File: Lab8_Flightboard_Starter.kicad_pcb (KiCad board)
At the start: 2 copper layers, 80 x 80 mm, 64 parts, among them J10 ESC3_GND, J11 ESC4_VBAT, J12 ESC4_GND, J5 ESC1_VBAT, J6 ESC1_GND, J7 ESC2_VBAT, J8 ESC2_GND, J9 ESC3_VBAT, M1 Motor1, M2 Motor2, M3 Motor3, M4 Motor4, Q1 DMP6023LE-13, U2 TPS62933, U4 LP5912-3.3DRV, U5 LP5912-3.3DRV, U6 NRF24L01_Breakout

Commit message: More traces
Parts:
- moved D6 38.2 mm to (130.0, 93.5), turned to 0 degrees
- moved D3 33.7 mm to (162.5, 103.5)
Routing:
- net /SCK: track 0.00 -> 55.8 mm, vias 0 -> 8
- net /CS: track 0.00 -> 52.0 mm, vias 0 -> 6
- net /3.3V_IMU: track 0.00 -> 47.1 mm
- net /M2_CMD: track 0.00 -> 37.2 mm, vias 0 -> 3
- net /M1_CMD: track 0.00 -> 36.7 mm, vias 0 -> 2
- net /MOSI: track 0.00 -> 22.5 mm, vias 0 -> 2
- net /5V_OUT: track 83.5 -> 106.0 mm
- net /3.3V_GP: track 0.00 -> 17.7 mm
- net /MISO: track 0.00 -> 14.1 mm, vias 0 -> 3
- net /MOTOR2: track 0.00 -> 9.83 mm
- net /ADC3: track 0.00 -> 9.70 mm
- net /MOTOR1: track 0.00 -> 8.21 mm
- net Net-(D3-A): track 0.00 -> 2.97 mm
- net Net-(D6-A): track 0.00 -> 2.64 mm

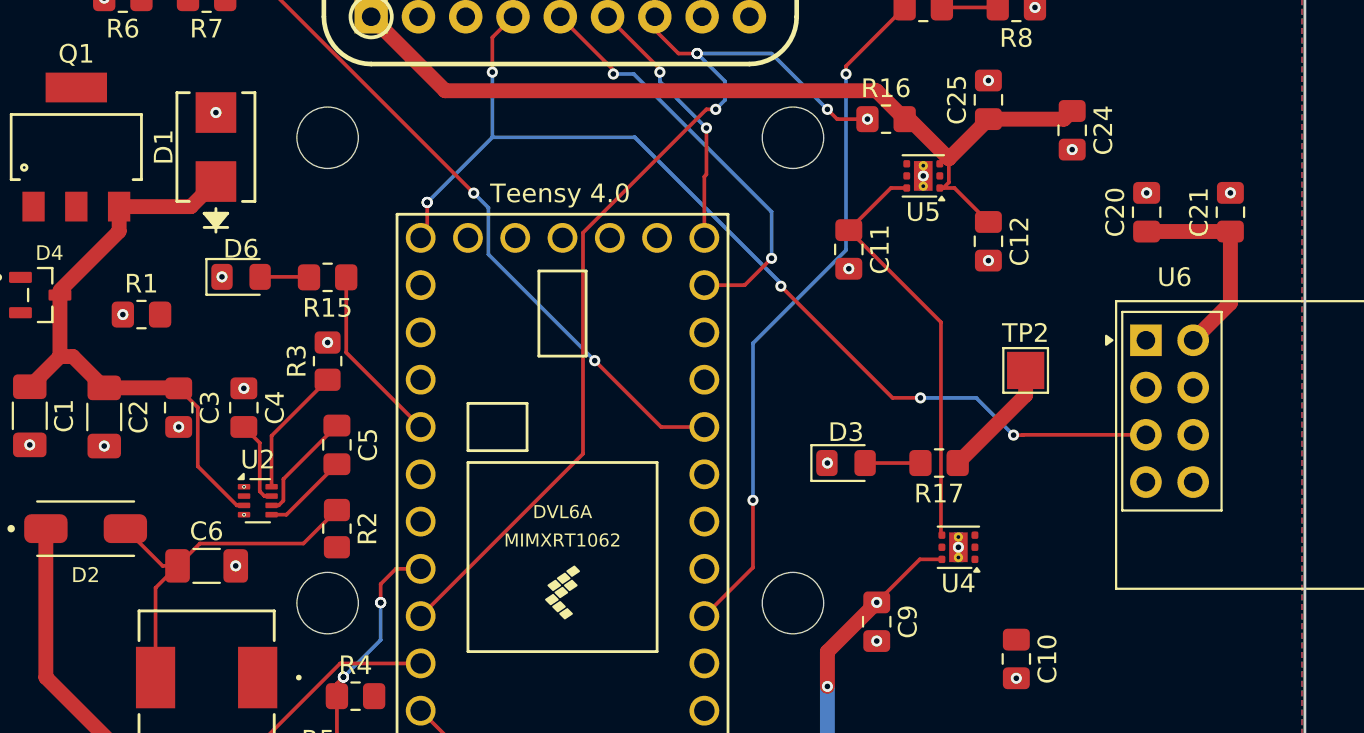
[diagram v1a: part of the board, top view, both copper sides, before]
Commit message: Added all traces (errors still)
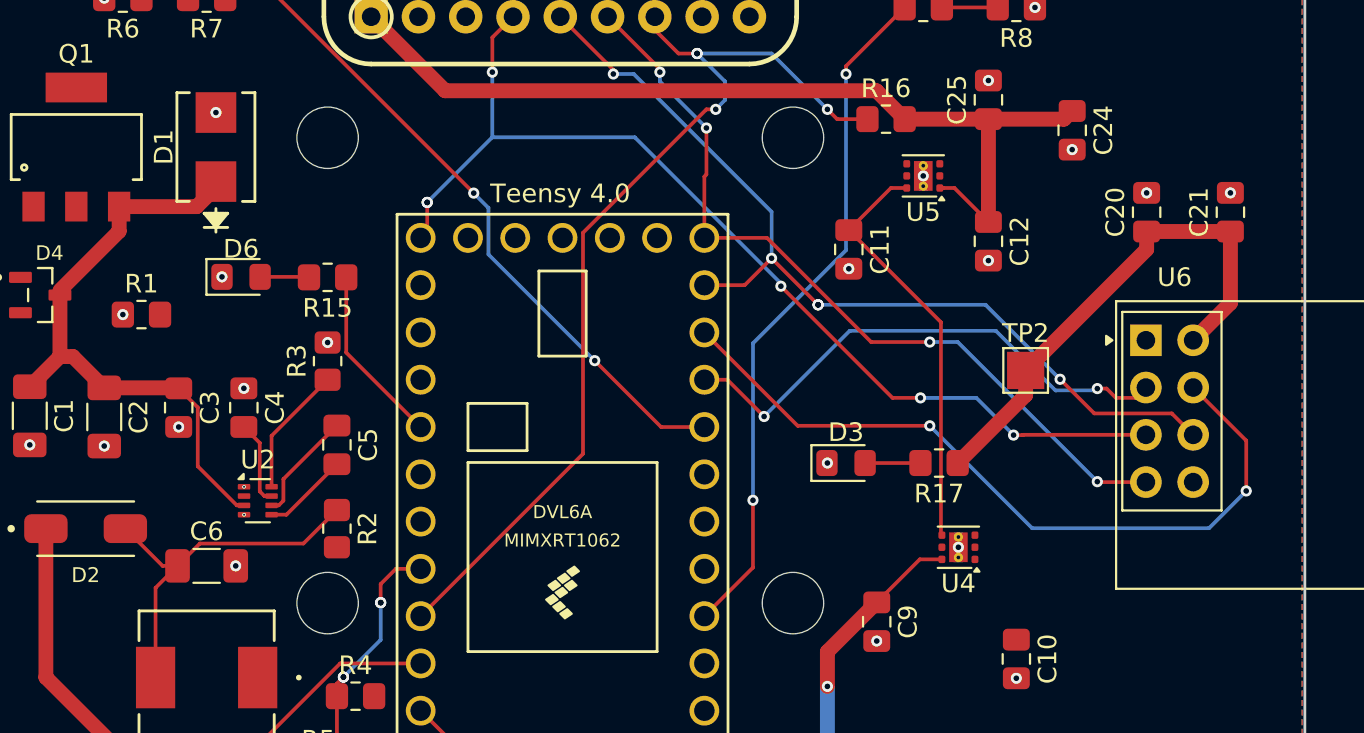
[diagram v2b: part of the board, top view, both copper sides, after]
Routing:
- net /CSN: track 0.00 -> 41.0 mm, vias 0 -> 2
- net /MISO: track 14.1 -> 43.3 mm, vias 3 -> 4
- net /CE: track 0.00 -> 28.2 mm, vias 0 -> 2
- net /MOSI: track 22.5 -> 49.1 mm, vias 2 -> 5
- net /3.3V_GP: track 17.7 -> 27.8 mm
- net /3.3V_IMU: track 47.1 -> 49.2 mm
- net /SCK: vias 8 -> 6
- net /M2_CMD: vias 3 -> 2
- net /CS: vias 6 -> 5
- net /5V_OUT: vias 5 -> 4

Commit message: Fixed most errors
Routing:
- net /VBAT: track 0.00 -> 16.5 mm
- net /3.3V_GP: track 27.8 -> 41.3 mm
- net Net-(D4-~-Pad1): track 0.00 -> 13.3 mm, vias 0 -> 2
- net Net-(U2-SW): track 4.63 -> 13.5 mm, vias 0 -> 2
- net /MOTOR3: track 2.00 -> 7.68 mm
- net Net-(U2-BST): track 5.96 -> 11.6 mm
- net Net-(U2-FB): track 7.00 -> 12.4 mm, vias 0 -> 2
- net GND: track 0.00 -> 4.53 mm
- net /CE: track 28.2 -> 32.5 mm
- net /5V_OUT: track 106.0 -> 109.4 mm
- net /VBAT_SENSE: vias 4 -> 2
- net /SCK: vias 6 -> 5
- net /MOSI: vias 5 -> 4
- net /CS: vias 5 -> 3

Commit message: Fixed all errors
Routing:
- net /VBAT: track 16.5 -> 33.3 mm, vias 0 -> 2
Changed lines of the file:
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@@
 	)
 	(segment
-		(start 121.15 83.325)
-		(end 112.3 92.175)
+		(start 118.65 134.025)
+		(end 125.475 134.025)
 		(width 0.8)
 		(layer "F.Cu")
@@
 	)
 	(segment
-		(start 112.3 92.175)
-		(end 112.3 96.125)
-		(width 0.8)
-		(layer "F.Cu")
+		(start 116.5 131.875)
+		(end 118.65 134.025)
+		(width 0.8)
+		(layer "F.Cu")
+		(net "/VBAT")
+	)
+	(segment
+		(start 125.475 134.025)
+		(end 134 125.5)
+		(width 0.8)
+		(layer "F.Cu")
+		(net "/VBAT")
+	)
+	(segment
+		(start 134 125.5)
+		(end 135 125.5)
+		(width 0.8)
+		(layer "F.Cu")
+		(net "/VBAT")
+	)
+	(segment
+		(start 137.15 116.025)
+		(end 137.15 120.35)
+		(width 0.8)
+		(layer "F.Cu")
+		(net "/VBAT")
+	)
+	(segment
+		(start 137.15 120.35)
+		(end 137 120.5)
+		(width 0.2)
+		(layer "F.Cu")
+		(net "/VBAT")
+	)
+	(via
+		(at 137 120.5)
+		(size 0.6)
+		(drill 0.3)
+		(layers "F.Cu" "B.Cu")
+		(net "/VBAT")
+	)
+	(via
+		(at 135 125.5)
+		(size 0.6)
+		(drill 0.3)
+		(layers "F.Cu" "B.Cu")
+		(net "/VBAT")
+	)
+	(segment
+		(start 135.5 125)
+		(end 135 125.5)
+		(width 0.8)
+		(layer "B.Cu")
+		(net "/VBAT")
+	)
+	(segment
+		(start 137 120.5)
+		(end 135.5 122)
+		(width 0.8)
+		(layer "B.Cu")
+		(net "/VBAT")
+	)
+	(segment
+		(start 135.5 122)
+		(end 135.5 125)
+		(width 0.8)
+		(layer "B.Cu")
 		(net "/VBAT")
 	)
@@
 		(polygon
 			(pts
-				(xy 107 59.5) (xy 108 58.5) (xy 186.5 58.5) (xy 187 59.5) (xy 187 138) (xy 186 138.5) (xy 108 138.5)
+				(xy 107 59.5) (xy 108 58.5) (xy 186.5 58.5) (xy 187 59.5) (xy 187 137.5) (xy 186 138.5) (xy 108 138.5)
 				(xy 107 137.5)
 			)

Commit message: Added BOM and gerber
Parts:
- renumbered LSM to U9
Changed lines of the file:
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@@
 		(descr "Adafruit LSM6DSO32 6-DoF IMU breakout, product 4692; 25.4 x 17.78 mm; 1x9 primary and 1x5 auxiliary 2.54 mm headers.")
 		(tags "Adafruit LSM6DSO32 breakout IMU I2C SPI STEMMA QT")
-		(property "Reference" "LSM"
+		(property "Reference" "U9"
 			(at 0 -10.4 0)
 			(layer "F.SilkS")

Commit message: Fixed values
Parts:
- L1: value 3.3u -> 4.7u
- U1: renamed from Teensy 4.0
- renumbered M1 to J1, M2 to J2, M3 to J3, M4 to J4

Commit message: Edited formatting and remade BOM
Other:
- board text added: "LP"
- board text added: "LSM"
- board text added: "Motor1"
- board text added: "Motor2"
- board text added: "Motor3"
- board text added: "Motor4"
- board text added: "NRF"
- board text added: "TPS"
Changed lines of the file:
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@@
 		(tags "nRF24L01 adapter breakout")
 		(property "Reference" "U6"
-			(at 1.54 -3.38 0)
+			(at 1.54 -2.905 0)
 			(layer "F.SilkS")
+			(hide yes)
 			(effects
 				(font
@@
 			(at 2.475 2.5 0)
 			(layer "F.SilkS")
+			(hide yes)
 			(effects
 				(font
@@
 		(tags "resistor handsolder")
 		(property "Reference" "R17"
-			(at 0 -1.65 0)
+			(at 0 1.5 0)
 			(layer "F.SilkS")
 			(effects
@@
 		(tags "capacitor handsolder")
 		(property "Reference" "C15"
-			(at 0 -1.68 90)
+			(at 0 1.65 90)
 			(layer "F.SilkS")
 			(effects
@@
 		(tags "capacitor handsolder")
 		(property "Reference" "C1"
-			(at 0 -1.85 90)
+			(at -2.9625 0.05 180)
 			(layer "F.SilkS")
 			(effects
@@
 		(tags "capacitor handsolder")
 		(property "Reference" "C10"
-			(at 0 -1.68 90)
+			(at 0 1.65 90)
 			(layer "F.SilkS")
 			(effects
@@
 			(at 0 -2.225 0)
 			(layer "F.SilkS")
+			(hide yes)
 			(effects
 				(font
@@
 			(layer "F.Fab")
 		)
-		(fp_text user "${REFERENCE}"
-			(at 0 0 0)
-			(layer "F.Fab")
-			(effects
-				(font
-					(size 0.5 0.5)
-					(thickness 0.08)
-				)
-			)
-		)
 		(pad "" smd roundrect
 			(at 0 -0.4 180)
@@
 		(tags "resistor handsolder")
 		(property "Reference" "R8"
-			(at 0 -1.65 0)
+			(at 0.15 1.525 0)
 			(layer "F.SilkS")
 			(effects
@@
 		(tags "capacitor handsolder")
 		(property "Reference" "C3"
-			(at 0 -1.68 90)
+			(at -2.525 0.05 180)
 			(layer "F.SilkS")
 			(effects
@@
 			(at 0 -10.4 0)
 			(layer "F.SilkS")
+			(hide yes)
 			(effects
 				(font
@@
 			)
 		)
-		(property "Datasheet" "https://www.adafruit.com/product/4692"
+		(property "Datasheet" ""
 			(at 0 0 0)
 			(layer "F.Fab")
@@
 			)
 		)
-		(property "Description" "Adafruit LSM6DSO32 6-DoF accelerometer/gyroscope breakout; I2C/SPI, STEMMA QT, primary and auxiliary headers."
+		(property "Description" ""
 			(at 0 0 0)
 			(layer "F.Fab")
@@
 		(tags "capacitor handsolder")
 		(property "Reference" "C2"
-			(at 0 -1.85 90)
+			(at -3.025 0.05 180)
 			(layer "F.SilkS")
 			(effects
@@
 		(tags "SMBJ17A ")
 		(property "Reference" "D1"
-			(at 0 -2.7987 90)
+			(at 4.025 -0.05 0)
 			(unlocked yes)
 			(layer "F.SilkS")
@@
 		(tags "resistor handsolder")
 		(property "Reference" "R2"
-			(at 0 -1.65 90)
+			(at -0.025 1.65 90)
 			(layer "F.SilkS")
 			(effects
@@
 		(tags "WSON NoLead")
 		(property "Reference" "U4"
-			(at 0 -1.95 0)
+			(at 0 2.025 0)
 			(layer "F.SilkS")
+			(hide yes)
 			(effects
 				(font
@@
 		(tags "Through hole pin header THT 1x03 2.54mm single row")
 		(property "Reference" "J2"
-			(at -2.5 2.85 180)
+			(at -2.475 2.35 180)
 			(layer "F.SilkS")
+			(hide yes)
 			(effects
 				(font
@@
 		(tags "capacitor handsolder")
 		(property "Reference" "C24"
-			(at 0 -1.68 90)
+			(at 0 1.65 90)
 			(layer "F.SilkS")
 			(effects
@@
 		(tags "resistor handsolder")
 		(property "Reference" "R12"
-			(at 0 -1.65 0)
+			(at 0 1.525 0)
 			(layer "F.SilkS")
 			(effects
@@
 			(at 2.475 2.5 180)
 			(layer "F.SilkS")
+			(hide yes)
 			(effects
 				(font
@@
 		(tags "capacitor handsolder")
 		(property "Reference" "C5"
-			(at 0 -1.68 90)
+			(at 0 1.65 90)
 			(layer "F.SilkS")
 			(effects
@@
 		(at 147.27 107.915 90)
 		(property "Reference" "U1"
-			(at 18.89 -0.12 180)
+			(at 0 -10.16 90)
 			(layer "F.SilkS")
+			(hide yes)
 			(effects
 				(font
@@
 		)
 		(property "Value" "Teensy4.0"
-			(at 0 10.16 90)
-			(layer "F.Fab")
-			(hide yes)
+			(at 18.915 0.23 180)
+			(layer "F.SilkS")
 			(effects
 				(font
@@
 			)
 		)
-		(property "Description" "Teensy 4.0 development board"
+		(property "Description" ""
 			(at 0 0 90)
 			(layer "F.Fab")
@@
 		)
 		(fp_text user "DVL6A"
-			(at 1.778 0 0)
+			(at 1.778 0 180)
 			(layer "F.SilkS")
 			(effects
@@
 		)
 		(fp_text user "MIMXRT1062"
-			(at 0.254 0 0)
+			(at 0.254 0 180)
 			(layer "F.SilkS")
 			(effects
@@
 		(tags "capacitor handsolder")
 		(property "Reference" "C14"
-			(at 0 -1.68 90)
+			(at -0.025 1.65 90)
 			(layer "F.SilkS")
 			(effects
@@
 		(tags "capacitor handsolder")
 		(property "Reference" "C4"
-			(at 0 -1.68 90)
+			(at -2.525 0.05 180)
 			(layer "F.SilkS")
 			(effects
@@
 			(unlocked yes)
 			(layer "F.SilkS")
+			(hide yes)
 			(effects
 				(font
@@
 		(at 121.65 107.025)
 		(property "Reference" "D2"
-			(at 0 2.5 0)
+			(at 0 -2.025 0)
 			(layer "F.SilkS")
 			(effects
@@
 			(at -2.5 2.5 180)
 			(layer "F.SilkS")
+			(hide yes)
 			(effects
 				(font
@@
 		(tags "resistor handsolder")
 		(property "Reference" "R11"
-			(at 0 -1.65 0)
+			(at 0 1.5 0)
 			(layer "F.SilkS")
 			(effects
@@
 		(tags "capacitor handsolder")
 		(property "Reference" "C9"
-			(at 0 -1.68 90)
+			(at 0 1.65 90)
 			(layer "F.SilkS")
 			(effects
@@
 		(tags "capacitor handsolder")
 		(property "Reference" "C11"
-			(at 0 -1.68 90)
+			(at 0 1.65 90)
 			(layer "F.SilkS")
 			(effects
@@
 		(tags "resistor handsolder")
 		(property "Reference" "R13"
-			(at 0 -1.65 0)
+			(at 0 -1.525 0)
 			(layer "F.SilkS")
 			(effects
@@
 		(layer "Edge.Cuts")
 	)
+	(gr_text "Motor1"
+		(at 124 70.5 0)
+		(layer "F.SilkS")
+		(effects
+			(font
+				(size 1 1)
+				(thickness 0.15)
+			)
+		)
+	)
+	(gr_text "Motor3"
+		(at 124 128 0)
+		(layer "F.SilkS")
+		(effects
+			(font
+				(size 1 1)
+				(thickness 0.15)
+			)
+		)
+	)
+	(gr_text "TPS"
+		(at 130.9 103.5 0)
+		(layer "F.SilkS")
+		(effects
+			(font
+				(size 1 1)
+				(thickness 0.15)
+			)
+		)
+	)
+	(gr_text "LSM"
+		(at 147.15 63.5 0)
+		(layer "F.SilkS")
+		(effects
+			(font
+				(size 1 1)
+				(thickness 0.15)
+			)
+		)
+	)
+	(gr_text "LP"
+		(at 166.65 90.3 0)
+		(layer "F.SilkS")
+		(effects
+			(font
+				(size 1 1)
+				(thickness 0.15)
+			)
+		)
+	)
+	(gr_text "LP"
+		(at 168.5375 106 0)
+		(layer "F.SilkS")
+		(effects
+			(font
+				(size 1 1)
+				(thickness 0.15)
+			)
+		)
+	)
+	(gr_text "Motor2"
+		(at 171 70.5 0)
+		(layer "F.SilkS")
+		(effects
+			(font
+				(size 1 1)
+				(thickness 0.15)
+			)
+		)
+	)
+	(gr_text "Motor4"
+		(at 171 128 0)
+		(layer "F.SilkS")
+		(effects
+			(font
+				(size 1 1)
+				(thickness 0.15)
+			)
+		)
+	)
+	(gr_text "NRF"
+		(at 180 111.5 0)
+		(layer "F.SilkS")
+		(effects
+			(font
+				(size 1 1)
+				(thickness 0.15)
+			)
+		)
+	)
 	(dimension

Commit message: Added BOM and gerber for 3.3u inductor
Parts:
- L1: value 4.7u -> 3.3u
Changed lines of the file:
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@@
 			)
 		)
-		(property "Value" "4.7u"
+		(property "Value" "3.3u"
 			(at 0 0 180)
 			(unlocked yes)
